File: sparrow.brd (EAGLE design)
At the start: 80 x 80 mm, 196 parts, among them IC1 LAN8720AVIAS, IC2 TLV320AIC3100VIAS, IC3 TPS2500, IC4 SKYWORKS_AAT4280ASC70JW-8-NOT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, IC5 SKYWORKS_AAT4280ASC70JW-8-NOT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, IC6 SKYWORKS_AAT4280ASC70JW-8-NOT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, IC7 SKYWORKS_AAT4280ASC70JW-8-NOT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, IC8 SKYWORKS_AAT4280ASC70JW-8-NOT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, IC9 FXMA10820-DFN, X1 ABS07-32768, X2 12MHz, X3 32768, X4 50MHZ, X5 16MHz

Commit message: moved artwork
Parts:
- moved LOGO2 3.20 mm to (50.6, 30.0)
- moved LOGO3 1.20 mm to (31.6, 30.0)
- moved LOGO4 0.50 mm to (12.6, 30.0)
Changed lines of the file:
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@@
 <attribute name="NAME" x="1.0588" y="69.5238" size="0.8" layer="25" font="vector" ratio="10"/>
 </element>
-<element name="LOGO2" library="anykey" package="LOGO-KRONE" value="LOGOKRONE" x="53.8" y="30" rot="MR180"/>
-<element name="LOGO3" library="anykey" package="LOGO-KRONE" value="LOGOKRONE" x="32.8" y="30" rot="MR180"/>
-<element name="LOGO4" library="anykey" package="LOGO-KRONE" value="LOGOKRONE" x="12.1" y="30" rot="MR180"/>
+<element name="LOGO2" library="anykey" package="LOGO-KRONE" value="LOGOKRONE" x="50.6" y="30" rot="MR180"/>
+<element name="LOGO3" library="anykey" package="LOGO-KRONE" value="LOGOKRONE" x="31.6" y="30" rot="MR180"/>
+<element name="LOGO4" library="anykey" package="LOGO-KRONE" value="LOGOKRONE" x="12.6" y="30" rot="MR180"/>
 <element name="R40" library="anykey" package="0603" value="33" x="48" y="37.8" smashed="yes">
 <attribute name="NAME" x="47.078" y="38.354" size="0.8" layer="25" font="vector"/>
@@
 <via x="43.8" y="45.1" extent="1-16" drill="0.3"/>
 <via x="48.6" y="33" extent="1-16" drill="0.3"/>
-<via x="44.3" y="14" extent="1-16" drill="0.3"/>
+<via x="44" y="14" extent="1-16" drill="0.3"/>
 <via x="36.7" y="61.3" extent="1-16" drill="0.3"/>
 <via x="52.9" y="60.3" extent="1-16" drill="0.3"/>
@@
 <wire x1="71.45" y1="44.6" x2="69.4" y2="44.6" width="0.5" layer="1"/>
 <wire x1="71.45" y1="44.6" x2="73.6" y2="44.6" width="0.5" layer="1"/>
-<via x="38.3" y="14" extent="1-16" drill="0.3"/>
+<via x="36" y="14" extent="1-16" drill="0.3"/>
 <via x="25.8" y="5.7" extent="1-16" drill="0.3"/>
 <via x="56.1" y="6.9" extent="1-16" drill="0.3"/>

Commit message: RC1
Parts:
- added HEADPHONE: AUDIOJACK-STEREO-3PCUI_SJ_3523, anykey:CUI_SJ_3523_SMT
- I2S: value HEADER-1X10ROUND -> HEADER-2X5SMD-1.27MM; device anykey:1X10_ROUND -> anykey:2X05_SMT
- moved MCLK 9.36 mm to (61.7, 36.5), turned to 270 degrees
- moved RX_SCK 8.12 mm to (60.4, 36.5), turned to 270 degrees
- moved TX_SCK 6.89 mm to (59.1, 36.5), turned to 270 degrees
- moved LS 5.68 mm to (78.1, 26.0)
- moved MIC 5.68 mm to (75.6, 26.0)
- moved RX_WS 5.65 mm to (57.8, 36.5), turned to 270 degrees
- moved C46 5.59 mm to (64.5, 35.3)
- moved C47 5.55 mm to (64.5, 36.6)
- moved I2S 5.33 mm to (61.5, 42.1), turned to 90 degrees
- moved TX_WS 4.42 mm to (56.5, 36.5), turned to 270 degrees
- moved RX_SD 3.20 mm to (55.2, 36.5), turned to 270 degrees
- moved HP 2.54 mm to (75.6, 19.7)
- moved LINE 2.54 mm to (78.1, 19.7)
- moved TX_SD 1.99 mm to (53.9, 36.5), turned to 270 degrees
- moved C40 1.20 mm to (64.0, 33.2)
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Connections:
- net MIC renamed N$4
- net GND: now also HEADPHONE.1
- net HP_L: now also HEADPHONE.2
- net HP_R: now also HEADPHONE.3
- net I2S_RX_MCLK: now also I2S.9; no longer I2S.3
- net I2S_RX_SCK: now also I2S.3; no longer I2S.4
- net I2S_RX_SD: now also I2S.7; no longer I2S.8
- net I2S_RX_WS: now also I2S.5; no longer I2S.6
- net I2S_TX_SCK: now also I2S.4; no longer I2S.5
- net I2S_TX_SD: now also I2S.8; no longer I2S.9
- net I2S_TX_WS: now also I2S.6; no longer I2S.7
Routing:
- net HP_L: track 3.72 -> 24.7 mm, vias 0 -> 1
- net HP_R: track 3.58 -> 22.6 mm, vias 0 -> 1
- net I2S_RX_WS: track 20.0 -> 31.7 mm, vias 1 -> 2
- net I2S_TX_MCLK: track 39.8 -> 51.0 mm, vias 1 -> 2
- net I2S_RX_SD: track 22.1 -> 30.5 mm, vias 1 -> 2
- net I2S_TX_SD: track 35.9 -> 43.6 mm, vias 1 -> 2
- net I2S_RX_SCK: track 24.8 -> 32.2 mm, vias 1 -> 2
- net SPKM: track 15.6 -> 21.6 mm
- net AUDIO_MCLK: track 25.1 -> 19.2 mm
- net VD33: track 595.4 -> 601.2 mm, vias 32 -> 33
- net N$4: track 15.4 -> 10.2 mm
- net SPKP: track 19.3 -> 24.3 mm
- net I2S_RX_MCLK: track 34.4 -> 30.0 mm, vias 1 -> 3
- net VAUDIO33: track 47.3 -> 51.2 mm
- net LINEIN1: track 8.54 -> 11.8 mm
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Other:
- board text removed: "TX_SD RX_SD TX_WS RX_WS TX_SCK RX_SCK MCLK GND 3V3"

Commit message: renamed library everykey
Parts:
- !PGM, RESET: device anykey:CK-KMR2 -> everykey:CK-KMR2
- 5VDC_IN: device anykey:CUI_PJ_102BH -> everykey:CUI_PJ_102BH
- ADC, GPIO_5V, SPI0, UART3: device anykey:1X07_ROUND -> everykey:1X07_ROUND
- ANT1, ANT2, X1, X3: device anykey:1206_MINIMELF_COMBO -> everykey:1206_MINIMELF_COMBO
- A_SCL, A_SDA, MCLK, RX_SCK, RX_SD, RX_WS, SCL, SDA, TX_SCK, TX_SD, TX_WS, WL_EN: device anykey:0603_SOLDERJUMPER_CLOSED -> everykey:0603_SOLDERJUMPER_CLOSED
- BAL1: device anykey:ST_BAL_WLCSP -> everykey:ST_BAL_WLCSP
- BATT: device anykey:S2B-PH-SM4-TB -> everykey:S2B-PH-SM4-TB
- C1, C55, C61, C62, C63, C64, C66, C67, C68, C69, C72, L5, L6: device anykey:0402 -> everykey:0402
- C10, C11, C12, C13, C14, C15, C16, C17, C18, C19, C2, C20, C21, C22, C23, C24, C25, C26, C27, C28, C29, C3, C30, C31, C32, C33, C34, C35, C36, C37, C38, C39, C4, C40, C41, C42, C43, C44, C45, C46, C47, C48, C49, C5, C52, C53, C54, C56, C58, C6, C65, C7, C74, C75, C76, C77, C78, C79, C8, C80, C9, R1, R10, R11, R12, R13, R14, R15, R16, R17, R18, R19, R2, R20, R21, R22, R23, R24, R25, R26, R27, R28, R29, R3, R30, R31, R32, R33, R34, R35, R36, R37, R38, R39, R4, R40, R41, R42, R43, R44, R45, R5, R6, R7, R8, R9: device anykey:0603 -> everykey:0603
- C50, C51, C57, C59: device anykey:0805 -> everykey:0805
- C60: device anykey:1210_POLAR -> everykey:1210_POLAR
- CC_DEBUG, I2S, LPC_DEBUG, NRF_DEBUG: device anykey:2X05_SMT -> everykey:2X05_SMT
- D1, D2, D3, D4, D5: device anykey:SOD123FL -> everykey:SOD123FL
- ETH: device anykey:RJ45-RB1-125BAG1A -> everykey:RJ45-RB1-125BAG1A
- HEADPHONE: device anykey:CUI_SJ_3523_SMT -> everykey:CUI_SJ_3523_SMT
- HP, LINE: device anykey:1X03_ROUND -> everykey:1X03_ROUND
- I2C0, I2C1, UART_5V: device anykey:1X05_ROUND -> everykey:1X05_ROUND
- IC1: device anykey:QFN24-0.5-EP-VIAS -> everykey:QFN24-0.5-EP-VIAS
- IC2: device anykey:QFN32-0.5-EP-VIAS -> everykey:QFN32-0.5-EP-VIAS
- IC3: device anykey:SON10-0.5-EP-VIAS -> everykey:SON10-0.5-EP-VIAS
- IC4, IC5, IC6, IC7, IC8: device anykey:SC70JW-8-NOTHERMALS -> everykey:SC70JW-8-NOTHERMALS
- IC9: device anykey:FXMA108 -> everykey:FXMA108
- L1, L7: device anykey:INDUCTOR_40X40 -> everykey:INDUCTOR_40X40
- LED1, LED2, LED3, LED4: device anykey:0603_POLAR -> everykey:0603_POLAR
- LIM: device anykey:0603_SOLDERJUMPER_OPEN -> everykey:0603_SOLDERJUMPER_OPEN
- LOGO2, LOGO3, LOGO4: device anykey:LOGO-KRONE -> everykey:LOGO-KRONE
- LS, MIC: device anykey:1X02_ROUND -> everykey:1X02_ROUND
- MCU: device anykey:QFP144-0.5 -> everykey:QFP144-0.5
- MCU1: device anykey:QFN48_EP -> everykey:QFN48_EP
- PWR1: device anykey:LTC4080_DFN -> everykey:LTC4080_DFN
- SD_CARD: device anykey:AMPHENO_101_00313_EXT_PADS -> everykey:AMPHENO_101_00313_EXT_PADS
- UART2: device anykey:1X06_ROUND -> everykey:1X06_ROUND
- USB0, USB1: device anykey:USB_MICRO_SMD -> everykey:USB_MICRO_SMD
- WIFI: device anykey:CC3000-EXT -> everykey:CC3000-EXT
- X2: device anykey:ABM8G -> everykey:ABM8G
- X4, X5: device anykey:CRYSTAL25X20 -> everykey:CRYSTAL25X20

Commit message: phy capacitors
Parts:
- C24, C25, C26: value 100n -> 10n
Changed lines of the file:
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@@
 <attribute name="NAME" x="68.446" y="55.878" size="0.8" layer="25" font="vector" rot="R90"/>
 </element>
-<element name="C24" library="everykey" package="0603" value="100n" x="56.3" y="53.2" smashed="yes" rot="R180">
+<element name="C24" library="everykey" package="0603" value="10n" x="56.3" y="53.2" smashed="yes" rot="R180">
 <attribute name="NAME" x="55.278" y="51.854" size="0.8" layer="25" font="vector"/>
 </element>
-<element name="C25" library="everykey" package="0603" value="100n" x="64.5" y="54.8" smashed="yes">
+<element name="C25" library="everykey" package="0603" value="10n" x="64.5" y="54.8" smashed="yes">
 <attribute name="NAME" x="63.322" y="55.246" size="0.8" layer="25" font="vector" rot="R180"/>
 </element>
-<element name="C26" library="everykey" package="0603" value="100n" x="61.4" y="47.6" smashed="yes" rot="R270">
+<element name="C26" library="everykey" package="0603" value="10n" x="61.4" y="47.6" smashed="yes" rot="R270">
 <attribute name="NAME" x="62.822" y="46.246" size="0.8" layer="25" font="vector" rot="R180"/>
 </element>

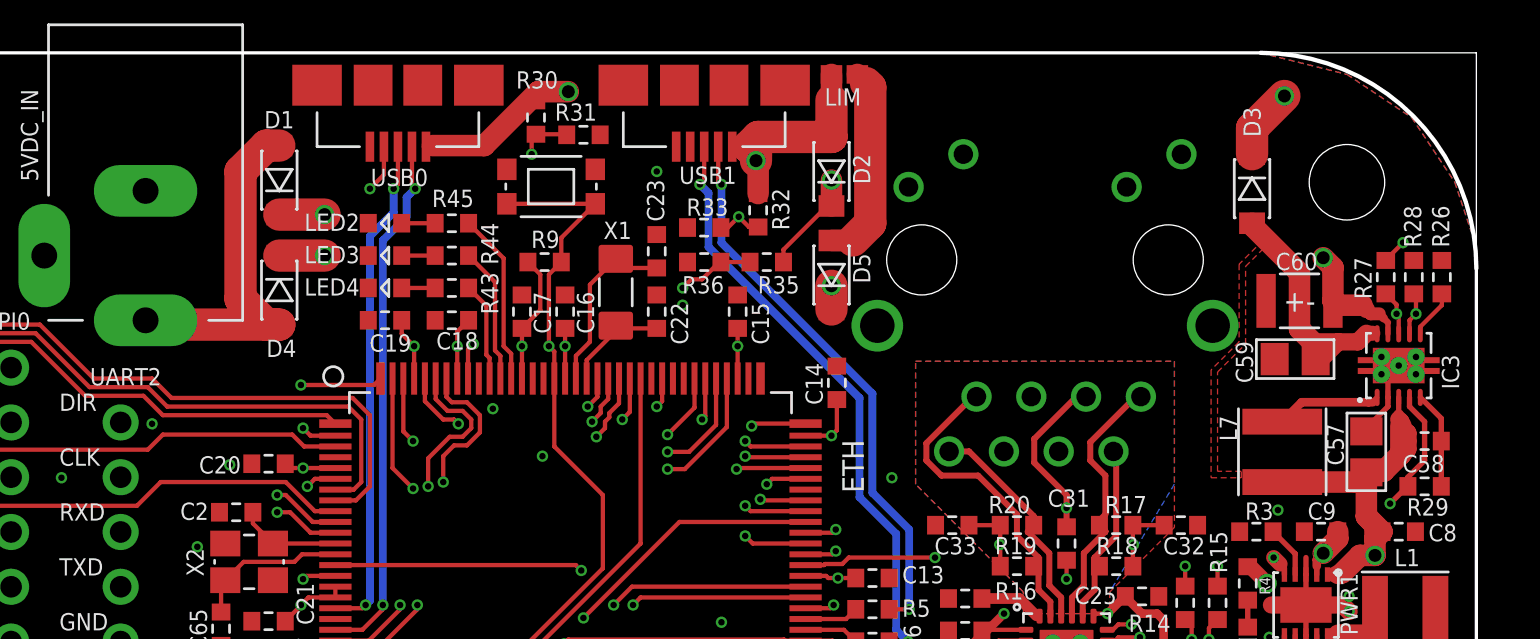
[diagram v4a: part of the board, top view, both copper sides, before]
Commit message: Added battery sensing
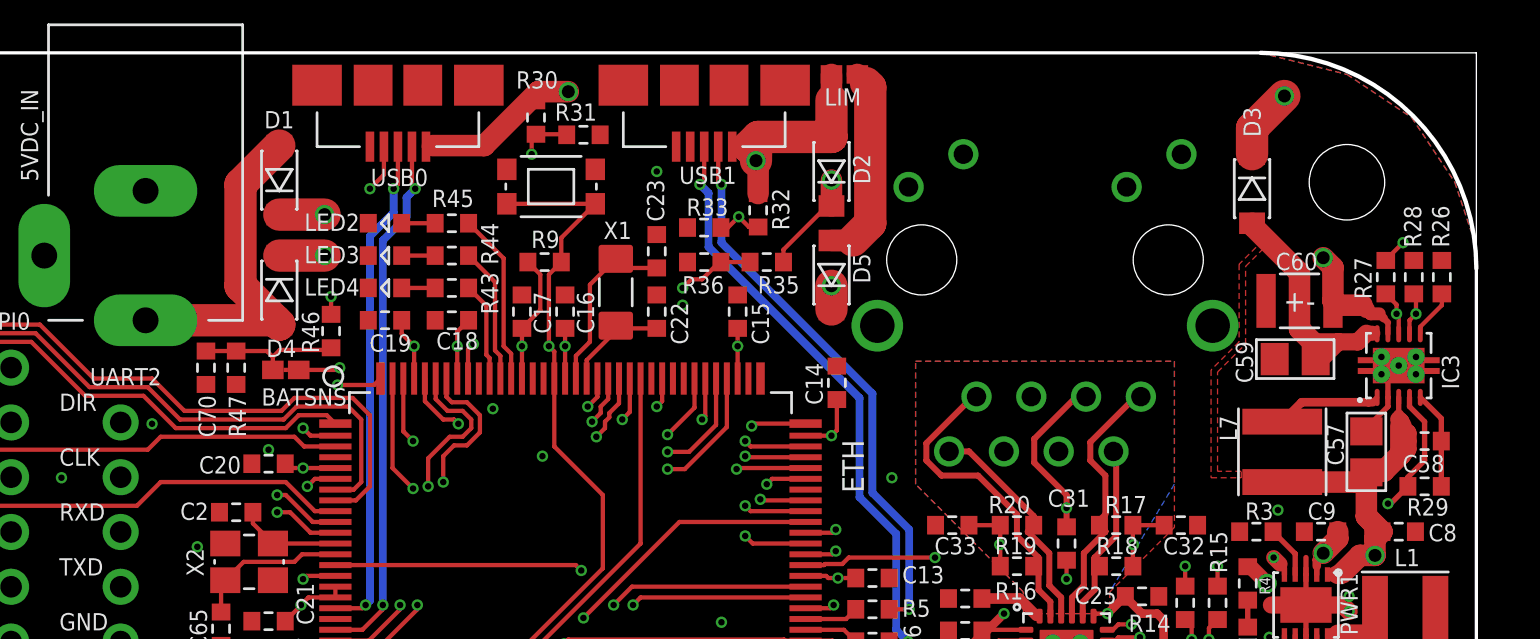
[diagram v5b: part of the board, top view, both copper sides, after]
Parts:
- added BATSNS: JUMPERSOLDER_CLOSED, everykey:0603_SOLDERJUMPER_CLOSED
- added C70: 100n, everykey:0603
- added R46, R47: 768K, everykey:0603
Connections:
- new net VBAT_SENSE: BATSNS.2, C70.1, R46.1, R47.2
- net ADC6: now also BATSNS.1
- net GND: now also C70.2, R47.1
- net VBAT: now also R46.2
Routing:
- net VBAT: track 35.5 -> 108.6 mm, vias 2 -> 3
- net VBAT_SENSE: track 0.00 -> 7.08 mm
- net ADC6: track 48.8 -> 50.1 mm, vias 1 -> 2
- net V5_OUT: track 216.2 -> 216.9 mm
- net VPOWER: track 16.8 -> 16.1 mm
- net ADC4: track 59.8 -> 59.2 mm
- net ADC3: track 61.4 -> 60.9 mm
- net ADC2: track 60.9 -> 60.3 mm
- net ADC0: track 57.1 -> 56.5 mm
- net ADC1: track 52.7 -> 52.1 mm
- net ADC5: track 46.3 -> 45.7 mm
